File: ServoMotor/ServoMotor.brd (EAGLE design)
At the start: 78.7 x 50.5 mm, 30 parts, among them Q1 TIP120, Q2 TIP120, Y1 16MHz

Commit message: Updated ServoMotor
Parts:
- added 5V_REG1: LP2950CDT-5.0G, LP2950CDT-5.0G:TO229P990X238-4N
- added R11, R12: 2.2KΩ, eagle-ltspice:R1210
- added R7, R8: 3.3KΩ, eagle-ltspice:R1210
- moved PWR_SERVO 11.4 mm to (74.9, 22.9)
- moved C6 9.02 mm to (47.0, 49.7), turned to 0 degrees
- moved C9 8.13 mm to (52.1, 49.7)
- moved J1 6.35 mm to (43.2, 24.1)
- moved Q2 2.84 mm to (55.9, 33.0), turned to 180 degrees
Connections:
- new net N$5: OPTO1.3, R7.2
- new net N$7: Q2.1, R11.1, R7.1
- new net N$8: 5V_REG1.1, PWR_SERVO.1
- net N$2: now also R8.2; no longer Q1.1
- net N$3: now also Q1.1, R12.1, R8.1; no longer OPTO1.3, Q2.1
- net PWR_SERVO_VCC: now also 5V_REG1.3; no longer PWR_SERVO.1
- net SERVO_GND: now also 5V_REG1.2, 5V_REG1.4
- net SERVO_VCC: now also R11.2, R12.2
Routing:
- net N$8: track 0.00 -> 23.1 mm
- net N$7: track 0.00 -> 21.1 mm
- net PWR_SERVO_VCC: track 49.2 -> 33.8 mm
- net SERVO_GND: track 7.26 -> 22.2 mm
- net N$3: track 4.11 -> 18.4 mm
- net SERVO_VCC: track 13.0 -> 26.9 mm
- net 3VCC: track 41.9 -> 33.0 mm
- net 5VCC: track 128.9 -> 137.6 mm
- net SERVO_PWM: track 9.94 -> 14.3 mm
- net N$2: track 6.87 -> 10.1 mm
- net N$5: track 0.00 -> 2.42 mm

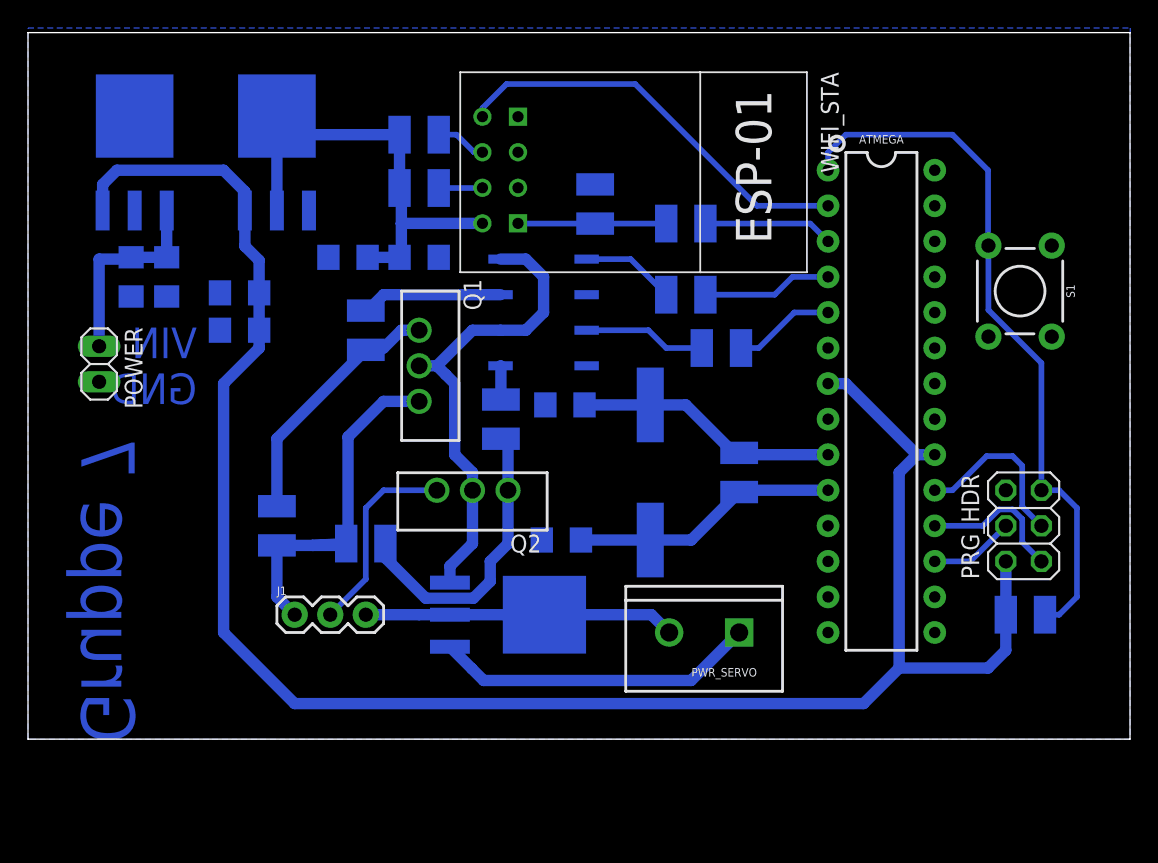
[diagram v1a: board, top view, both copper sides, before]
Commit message: Updated Boards, mainly changing up the Servomotor print due to cluttering
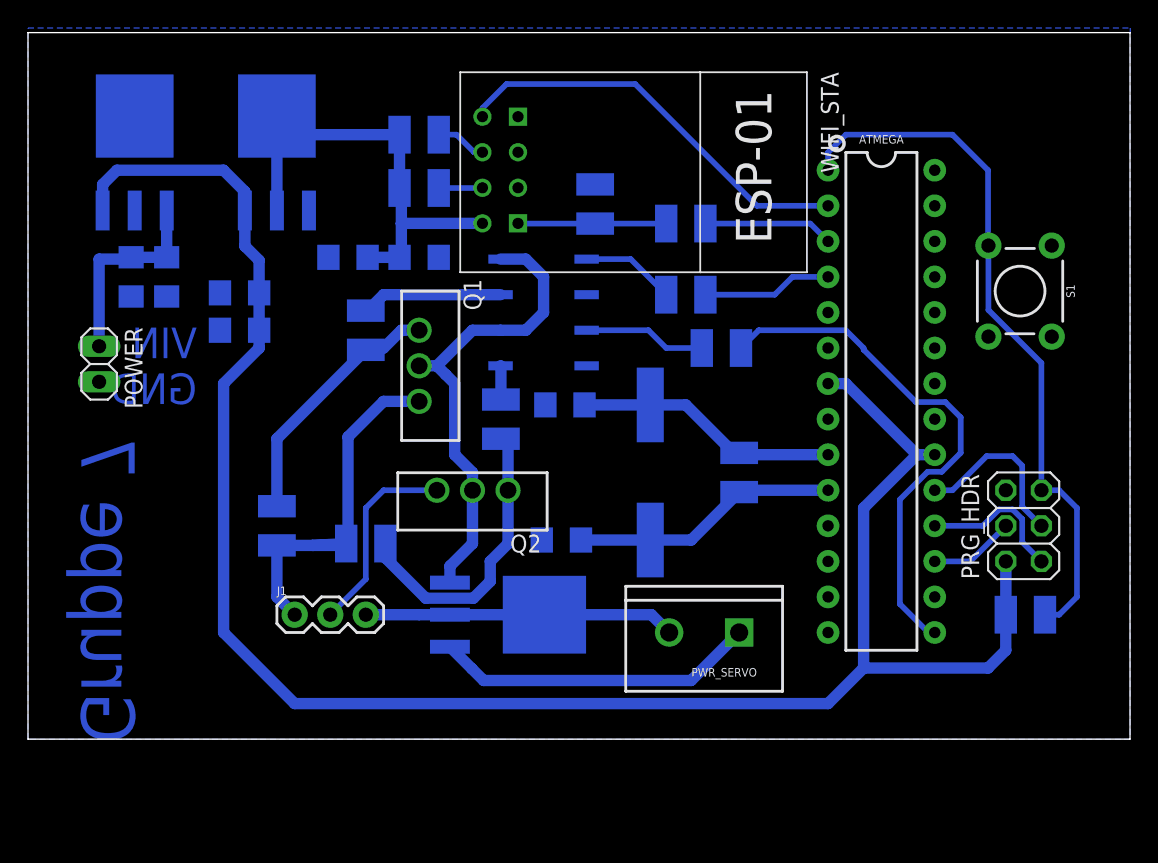
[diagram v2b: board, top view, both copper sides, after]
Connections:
- net GND: now also ATMEGA.5; no longer ATMEGA.15
- net N$4: now also ATMEGA.15; no longer ATMEGA.5
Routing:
- net N$4: track 7.27 -> 37.9 mm
- net 5VCC: track 137.6 -> 138.6 mm
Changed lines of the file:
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@@
 <contactref element="WIFI_STA" pad="GND"/>
 <contactref element="ATMEGA" pad="6"/>
-<contactref element="ATMEGA" pad="16"/>
-<contactref element="ATMEGA" pad="15"/>
 <contactref element="ATMEGA" pad="14"/>
 <contactref element="ATMEGA" pad="13"/>
@@
 <contactref element="OPTO" pad="2"/>
 <contactref element="OPTO1" pad="2"/>
+<contactref element="ATMEGA" pad="16"/>
+<contactref element="ATMEGA" pad="5"/>
 </signal>
 <signal name="3VCC" class="1">
@@
 <wire x1="87.63" y1="35.56" x2="82.55" y2="40.64" width="0.8128" layer="16"/>
 <wire x1="88.9" y1="35.56" x2="87.63" y2="35.56" width="0.8128" layer="16"/>
-<wire x1="87.63" y1="35.56" x2="86.36" y2="34.29" width="0.8128" layer="16"/>
-<wire x1="86.36" y1="34.29" x2="86.36" y2="20.32" width="0.8128" layer="16"/>
+<wire x1="87.63" y1="35.56" x2="83.82" y2="31.75" width="0.8128" layer="16"/>
+<wire x1="83.82" y1="31.75" x2="83.82" y2="20.32" width="0.8128" layer="16"/>
 <wire x1="38.103" y1="40.64" x2="38.103" y2="22.857" width="0.8128" layer="16"/>
 <wire x1="38.103" y1="22.857" x2="43.18" y2="17.78" width="0.8128" layer="16"/>
-<wire x1="86.36" y1="20.32" x2="92.71" y2="20.32" width="0.8128" layer="16"/>
+<wire x1="83.82" y1="20.32" x2="92.71" y2="20.32" width="0.8128" layer="16"/>
 <wire x1="92.71" y1="20.32" x2="93.977" y2="21.587" width="0.8128" layer="16"/>
 <wire x1="93.977" y1="21.587" x2="93.977" y2="24.13" width="0.8128" layer="16"/>
@@
 <wire x1="93.98" y1="24.133" x2="93.98" y2="27.94" width="0.8128" layer="16"/>
 <wire x1="40.643" y1="43.18" x2="38.103" y2="40.64" width="0.8128" layer="16"/>
-<wire x1="43.18" y1="17.78" x2="83.82" y2="17.78" width="0.8128" layer="16"/>
-<wire x1="83.82" y1="17.78" x2="86.36" y2="20.32" width="0.8128" layer="16"/>
+<wire x1="81.28" y1="17.78" x2="83.82" y2="20.32" width="0.8128" layer="16"/>
 <wire x1="40.643" y1="44.45" x2="40.643" y2="43.18" width="0.8128" layer="16"/>
+<wire x1="43.18" y1="17.78" x2="81.28" y2="17.78" width="0.8128" layer="16"/>
 </signal>
 <signal name="STA_TXD">
@@
 <wire x1="61.02" y1="24.13" x2="54.27" y2="24.13" width="0.8128" layer="16"/>
 </signal>
-<signal name="N$4">
-<contactref element="ATMEGA" pad="5"/>
-<contactref element="R5" pad="2"/>
-<wire x1="78.87" y1="45.72" x2="76.33" y2="43.18" width="0.4064" layer="16"/>
-<wire x1="75.06" y1="43.18" x2="76.33" y2="43.18" width="0.4064" layer="16"/>
-<wire x1="78.87" y1="45.72" x2="81.28" y2="45.72" width="0.4064" layer="16"/>
-</signal>
 <signal name="N$2">
 <contactref element="R8" pad="2"/>
@@
 <wire x1="55.835" y1="20.275" x2="55.835" y2="20.275" width="0.8128" layer="16"/>
 </signal>
+<signal name="N$4">
+<contactref element="ATMEGA" pad="15"/>
+<contactref element="R5" pad="2"/>
+<wire x1="88.3949875" y1="34.3408" x2="89.4050125" y2="34.3408" width="0.4064" layer="16"/>
+<wire x1="89.4050125" y1="34.3408" x2="90.7542" y2="35.6899875" width="0.4064" layer="16"/>
+<wire x1="90.7542" y1="35.6899875" x2="90.7542" y2="38.2240125" width="0.4064" layer="16"/>
+<wire x1="90.7542" y1="38.2240125" x2="89.6590125" y2="39.3192" width="0.4064" layer="16"/>
+<wire x1="88.4457875" y1="22.86" x2="86.4108" y2="24.8949875" width="0.4064" layer="16"/>
+<wire x1="86.4108" y1="32.3566125" x2="88.3949875" y2="34.3408" width="0.4064" layer="16"/>
+<wire x1="89.6590125" y1="39.3192" x2="87.560275" y2="39.3192" width="0.4064" layer="16"/>
+<wire x1="87.560275" y1="39.3192" x2="83.82" y2="43.059475" width="0.4064" layer="16"/>
+<wire x1="86.4108" y1="24.8949875" x2="86.4108" y2="32.3566125" width="0.4064" layer="16"/>
+<wire x1="88.9" y1="22.86" x2="88.4457875" y2="22.86" width="0.4064" layer="16"/>
+<wire x1="83.82" y1="43.059475" x2="83.82" y2="43.18" width="0.4064" layer="16"/>
+<wire x1="83.82" y1="43.18" x2="82.55" y2="44.45" width="0.4064" layer="16"/>
+<wire x1="82.55" y1="44.45" x2="76.33" y2="44.45" width="0.4064" layer="16"/>
+<wire x1="76.33" y1="44.45" x2="75.06" y2="43.18" width="0.4064" layer="16"/>
+</signal>
 </signals>

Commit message: wifitracker fix
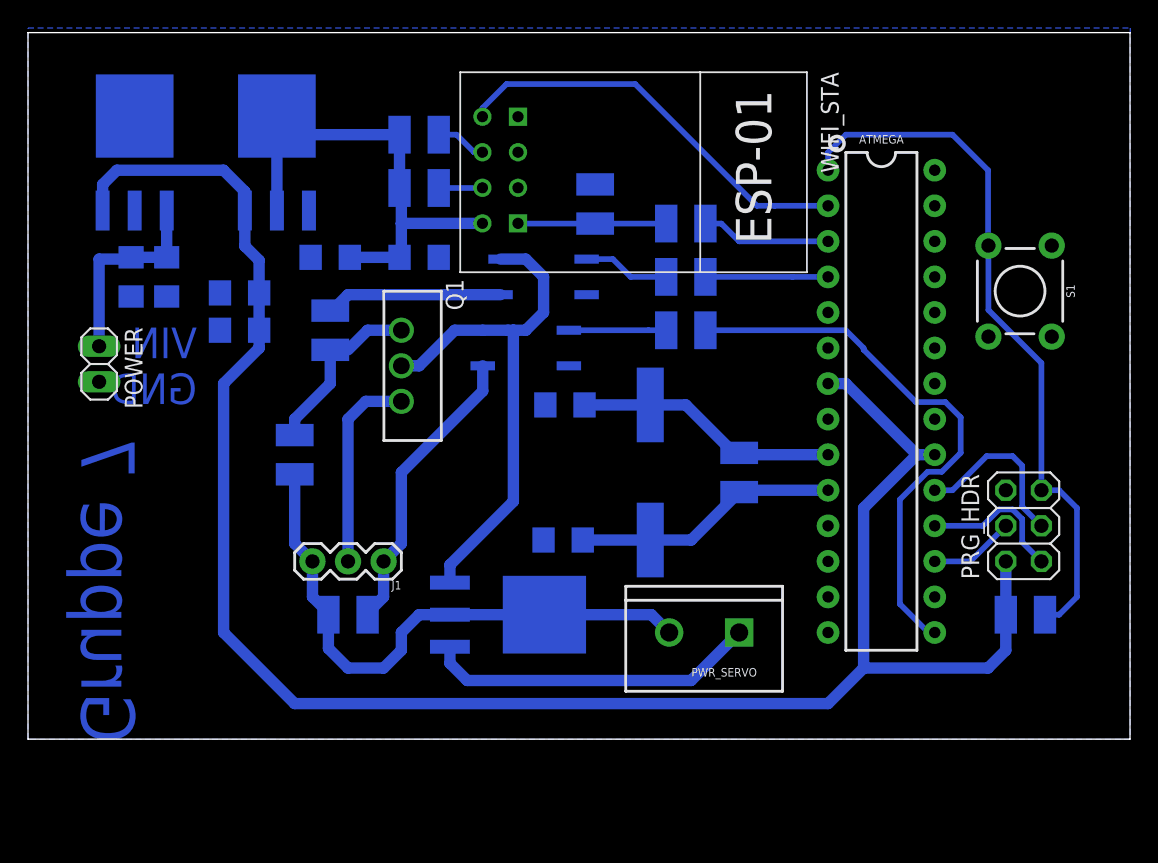
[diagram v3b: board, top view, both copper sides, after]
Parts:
- removed Q2: TIP120, TIP120:TO220
- removed R7: 3.3KΩ, eagle-ltspice:R1210
- R11: value 2.2KΩ -> 1KΩ
- R8: value 3.3KΩ -> 500Ω
- moved J1 7.41 mm to (49.5, 27.9), turned to 180 degrees
- moved R12 5.24 mm to (43.2, 35.6)
- moved R11 5.24 mm to (47.0, 24.1)
- moved R5 2.84 mm to (71.1, 44.5)
- moved R8 2.54 mm to (45.7, 44.5)
- moved C6 1.27 mm to (45.7, 49.7)
- moved OPTO1 1.27 mm to (59.7, 43.2)
- moved Q1 1.27 mm to (50.8, 41.9)
- moved R3 1.27 mm to (71.1, 48.3)
- moved C2 0.13 mm to (62.4, 29.5)
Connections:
- net N$3 renamed SERVO_VCC_BASE
- net N$4 renamed ATMEG_PWM
- net N$8 renamed BAT_SERVO_VCC
- removed net N$5: OPTO1.3, R7.2
- removed net N$7: Q2.1, R11.1, R7.1
- net PWR_SERVO_VCC: no longer Q2.2
- net SERVO_GND: now also R11.2, R12.2
- net SERVO_PWM: now also J1.1, OPTO1.3, R11.1; no longer J1.2, Q2.3
- net SERVO_VCC: now also J1.2; no longer J1.1, R11.2, R12.2
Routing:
- net N$7: track 21.1 -> 0.00 mm
- net SERVO_GND: track 22.2 -> 41.2 mm
- net SERVO_VCC: track 26.9 -> 14.5 mm
- net SERVO_PWM: track 14.3 -> 21.2 mm
- net SERVO_VCC_BASE: track 18.4 -> 11.5 mm
- net PWR_SERVO_VCC: track 33.8 -> 37.8 mm
- net N$2: track 10.1 -> 12.6 mm
- net N$5: track 2.42 -> 0.00 mm
- net ATMEG_PWM: track 37.9 -> 39.9 mm
- net N$1: track 8.75 -> 6.95 mm
- net 3VCC: track 33.0 -> 34.3 mm
- net BAT_SERVO_VCC: track 23.1 -> 23.8 mm
- net OPTO_ANODE: track 6.74 -> 6.21 mm
- net SERVO_EN: track 9.29 -> 8.76 mm
